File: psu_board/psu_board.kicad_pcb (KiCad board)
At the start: 2 copper layers, 50.5 x 108.5 mm, 27 parts, among them J1 Conn_02x08_Odd_Even, SW1 SW_SPST, U1 LM7812_TO220, U2 LM7805_TO220, U3 LM7912_TO220

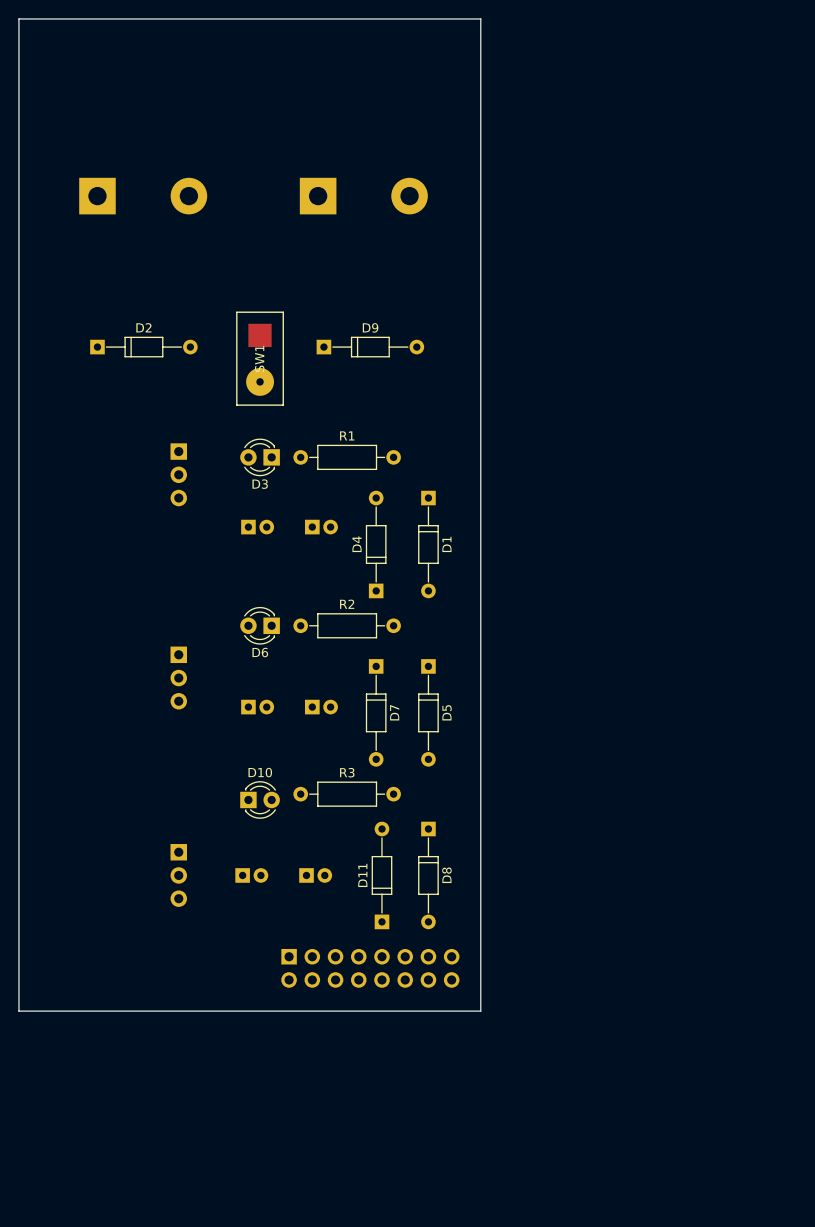
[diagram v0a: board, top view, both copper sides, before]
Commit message: added fuse holder
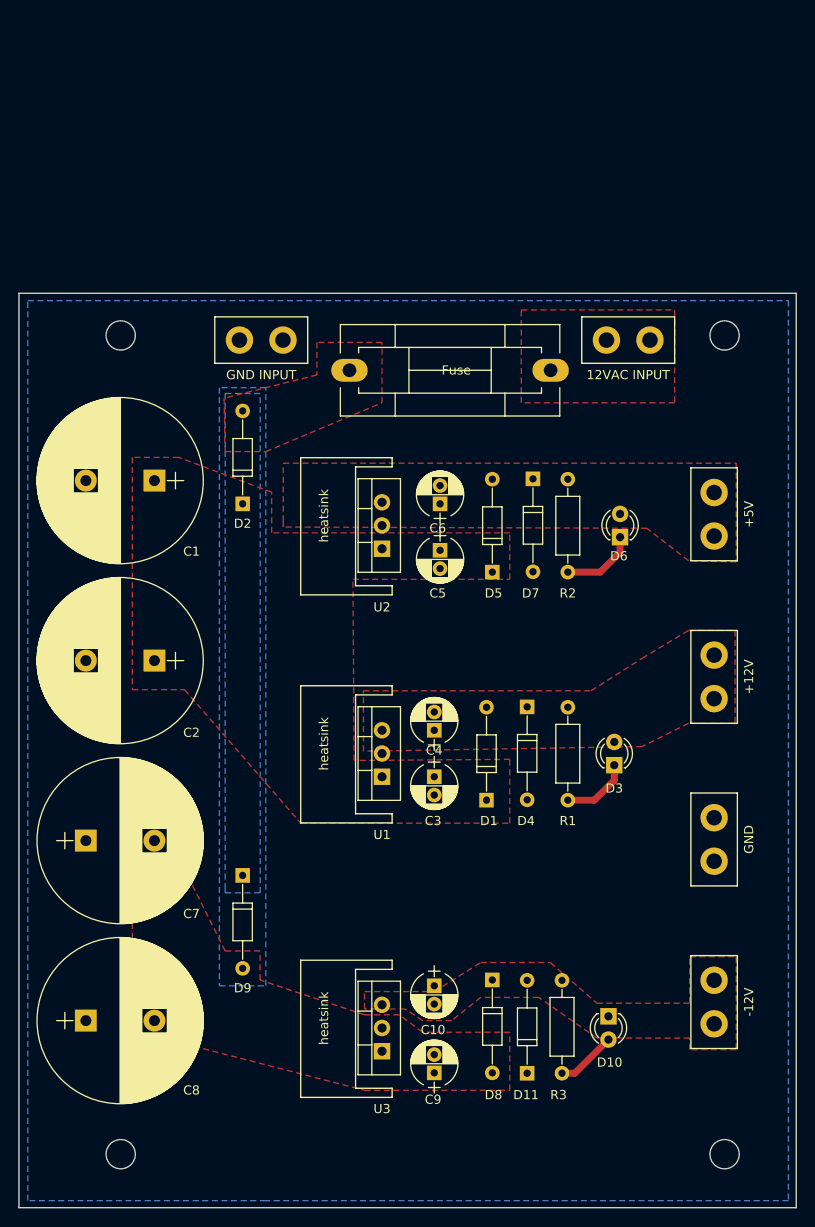
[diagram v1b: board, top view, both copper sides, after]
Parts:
- removed SW1: SW_SPST, Microwave:ALIM
- added C10: 1uF, Capacitors_THT:CP_Radial_D5.0mm_P2.00mm, F.Cu at (145.4, 125.7)
- added C9: 1uF, Capacitors_THT:CP_Radial_D5.0mm_P2.00mm, F.Cu at (145.4, 135.3)
- added F1: Fuse, Fuse_Holders_and_Fuses:Fuseholder5x20_horiz_SemiClosed_Casing10x25mm, F.Cu at (136.1, 58.4)
- added J2: +5V, digikey-footprints:spade_connector, F.Cu at (177.3, 74.2)
- added J3: +12V, digikey-footprints:spade_connector, F.Cu at (177.3, 91.9)
- added J4: GND, digikey-footprints:spade_connector, F.Cu at (177.3, 109.7)
- added J5: -12V, digikey-footprints:spade_connector, F.Cu at (177.3, 127.5)
- added J6: GND INPUT, digikey-footprints:spade_connector, F.Cu at (126.5, 56.4)
- added REF**: MountingHole_3.2mm_M3, Mounting_Holes:MountingHole_3.2mm_M3, F.Cu at (177.2, 54.6)
- added REF**: MountingHole_3.2mm_M3, Mounting_Holes:MountingHole_3.2mm_M3, F.Cu at (111.1, 54.6)
- added REF**: MountingHole_3.2mm_M3, Mounting_Holes:MountingHole_3.2mm_M3, F.Cu at (111.1, 144.1)
- added REF**: MountingHole_3.2mm_M3, Mounting_Holes:MountingHole_3.2mm_M3, F.Cu at (177.2, 144.1)
- added heatsink: heatsink_25mm_10mm, digikey-footprints:heatsink_25mm_10mm, F.Cu at (130.8, 122.9)
- added heatsink: heatsink_25mm_10mm, digikey-footprints:heatsink_25mm_10mm, F.Cu at (130.8, 92.9)
- added heatsink: heatsink_25mm_10mm, digikey-footprints:heatsink_25mm_10mm, F.Cu at (130.8, 68.0)
- C1: value 10000uF -> 4700uF; footprint Capacitors_THT:CP_Radial_D22.0mm_P10.00mm_SnapIn -> Capacitors_THT:CP_Radial_D18.0mm_P7.50mm; moved to F.Cu
- C2, C7, C8: value 1uF -> 4700uF; footprint Capacitors_THT:CP_Radial_D5.0mm_P2.00mm -> Capacitors_THT:CP_Radial_D18.0mm_P7.50mm; moved to F.Cu
- C3, C4, C5, U1, U2, U3: moved to F.Cu
- C6: value 10000uF -> 1uF; footprint Capacitors_THT:CP_Radial_D22.0mm_P10.00mm_SnapIn -> Capacitors_THT:CP_Radial_D5.0mm_P2.00mm; moved to F.Cu
- J1: value Conn_02x08_Odd_Even -> 12VAC INPUT; footprint Pin_Headers:Pin_Header_Straight_2x08_Pitch2.54mm -> digikey-footprints:spade_connector; moved to F.Cu
- moved J1 75.9 mm to (166.6, 56.4), turned to 0 degrees
- moved D9 58.5 mm to (124.5, 113.7), turned to 270 degrees
- moved D3 50.4 mm to (165.1, 101.6), turned to 90 degrees
- moved R1 47.5 mm to (160.0, 105.4), turned to 90 degrees
- moved D10 45.9 mm to (164.5, 129.1), turned to 270 degrees
- moved U1 41.9 mm to (139.7, 102.9), turned to 90 degrees
- moved R3 41.8 mm to (159.4, 135.3), turned to 90 degrees
- moved D6 39.3 mm to (165.7, 76.7), turned to 90 degrees
- moved C6 36.2 mm to (146.1, 73.0), turned to 90 degrees
- moved D1 33.6 mm to (151.1, 105.4), turned to 90 degrees
- moved C1 31.7 mm to (114.8, 70.5), turned to 180 degrees
- moved U3 31.1 mm to (139.7, 132.9), turned to 90 degrees
- moved C3 30.4 mm to (145.4, 102.9), turned to 270 degrees
- moved R2 29.8 mm to (160.0, 80.5), turned to 90 degrees
- moved C8 28.9 mm to (107.3, 129.5)
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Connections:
- C3 pad 1: +12V -> Net-(C1-Pad1)
- C4 pad 1: Net-(C1-Pad1) -> +12V
- C5 pad 1: Net-(C5-Pad1) -> Net-(C1-Pad1)
- C6 pad 1: GND -> +5V
- C6 pad 2: Net-(C6-Pad2) -> GND
- C7 pad 2: Net-(C6-Pad2) -> Net-(C7-Pad2)
- C8 pad 2: -12V -> Net-(C7-Pad2)
- D5 pad 2: Net-(C5-Pad1) -> +5V
- D6 pad 2: Net-(C5-Pad1) -> +5V
- D7 pad 1: Net-(C5-Pad1) -> +5V
- D8 pad 1: Net-(C6-Pad2) -> -12V
- D8 pad 2: -12V -> Net-(C7-Pad2)
- D9 pad 2: Net-(C6-Pad2) -> Net-(C7-Pad2)
- J1 pad 1: Net-(J1-Pad1) -> +12VA
- J1 pad 2: Net-(J1-Pad2) -> +12VA
- U2 pad 3: Net-(C5-Pad1) -> +5V
- U3 pad 2: Net-(C6-Pad2) -> Net-(C7-Pad2)
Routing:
- net Net-(D6-Pad1): track 0.00 -> 8.27 mm
- net Net-(D3-Pad1): track 0.00 -> 7.63 mm
- net Net-(D10-Pad2): track 0.00 -> 6.61 mm
- added copper zone on F.Cu, net +12V
- added copper zone on F.Cu, net +12VA
- added copper zone on F.Cu, net +5V
- added copper zone on F.Cu, net -12V
- added copper zone on B.Cu, net GND
- added copper zone on F.Cu, net Net-(C1-Pad1)
- added copper zone on F.Cu, net Net-(C7-Pad2)
- added copper zone on B.Cu, net Net-(D2-Pad2)
- added copper zone on F.Cu, net Net-(D2-Pad2)
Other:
- board size 50.5 x 108.5 mm -> 85 x 100 mm
- net class Default: trace_width 0.25 -> 1
